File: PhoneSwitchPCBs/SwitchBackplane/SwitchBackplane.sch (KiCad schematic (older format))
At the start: 255 parts, among them J1 Power, J10 UART, J11 SWD, J12 Station 4, J13 Station 8, J2 Station 1, J3 Station 5, J4 Trunk 1, J5 Station 2, J6 Station 6, J7 Trunk 2, J8 Station 3, J9 Station 7, Q1 XP231N02013R-G, Q10 XP231N02013R-G, Q11 XP231N02013R-G, Q12 PMV65XP, Q2 XP231N02013R-G, Q3 XP231N02013R-G, Q4 XP231N02013R-G, Q5 XP231N02013R-G, Q6 XP231N02013R-G, Q7 XP231N02013R-G, Q8 XP231N02013R-G, Q9 XP231N02013R-G, T1 FS28-200-C2, U1 Pi Pico, U10 XRA1403IG24TR-F, U11 TL071, U12 TL071, U13 XRA1403IG24TR-F, U14 XRA1403IG24TR-F, U15 XRA1403IG24TR-F, U2 TL074, U3 TL074, U4 74HC4316, U5 TL071, U6 MT8870DS1, U7 TPA3144D2PWPR, U8 MT8870DS1, U9 74HC4316, Y1 3.579545 MHz

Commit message: Associate footprints with parts, other tweaks
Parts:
- C1, C20, C21, C22, C23, C24, C25, C26, C27, C29, C30, C33, C34, C36, C37, C38, C39, C40, C41, C46, C47, C54, C55, C58, C59: footprint (none) -> Capacitor_SMD:C_1206_3216Metric_Pad1.33x1.80mm_HandSolder
- C10, C15, C43, C44: footprint (none) -> Capacitor_SMD:C_0805_2012Metric_Pad1.18x1.45mm_HandSolder
- C11, C12, C13, C14, C16, C17, C18, C19, C2, C28, C3, C32, C4, C45, C48, C49, C5, C52, C53, C57, C6, C64, C65, C66, C7, C8, C9: footprint (none) -> Capacitor_SMD:C_0603_1608Metric_Pad1.08x0.95mm_HandSolder
- C31, C35: value 1u -> 4.7u; footprint (none) -> Capacitor_SMD:C_1206_3216Metric_Pad1.33x1.80mm_HandSolder
- C42, C56: footprint (none) -> Capacitor_THT:CP_Radial_D6.3mm_P2.50mm
- C50, C51: value 1n -> .001u; footprint (none) -> Capacitor_SMD:C_0603_1608Metric_Pad1.08x0.95mm_HandSolder
- D12, D14, D6: footprint (none) -> LED_SMD:LED_0603_1608Metric_Pad1.05x0.95mm_HandSolder
- D13: value RE1 -> RE6; footprint (none) -> LED_SMD:LED_0603_1608Metric_Pad1.05x0.95mm_HandSolder
- D15: value RT1 -> RT7; footprint (none) -> LED_SMD:LED_0603_1608Metric_Pad1.05x0.95mm_HandSolder
- D16: value RT1 -> RT2; footprint (none) -> LED_SMD:LED_0603_1608Metric_Pad1.05x0.95mm_HandSolder
- D17: value RE1 -> RE7; footprint (none) -> LED_SMD:LED_0603_1608Metric_Pad1.05x0.95mm_HandSolder
- D18: value RE1 -> RE2; footprint (none) -> LED_SMD:LED_0603_1608Metric_Pad1.05x0.95mm_HandSolder
- D19: value RT1 -> RT8; footprint (none) -> LED_SMD:LED_0603_1608Metric_Pad1.05x0.95mm_HandSolder
- D20: value RT1 -> RT3; footprint (none) -> LED_SMD:LED_0603_1608Metric_Pad1.05x0.95mm_HandSolder
- D21: value RE1 -> RE8; footprint (none) -> LED_SMD:LED_0603_1608Metric_Pad1.05x0.95mm_HandSolder
- D24: value RE1 -> RE3; footprint (none) -> LED_SMD:LED_0603_1608Metric_Pad1.05x0.95mm_HandSolder
- D25: value RT1 -> TRT1; footprint (none) -> LED_SMD:LED_0603_1608Metric_Pad1.05x0.95mm_HandSolder
- D26: value RT1 -> RT4; footprint (none) -> LED_SMD:LED_0603_1608Metric_Pad1.05x0.95mm_HandSolder
- D27: value RE1 -> TA1; footprint (none) -> LED_SMD:LED_0603_1608Metric_Pad1.05x0.95mm_HandSolder
- D28: value RE1 -> RE4; footprint (none) -> LED_SMD:LED_0603_1608Metric_Pad1.05x0.95mm_HandSolder
- D29: value RT1 -> TRT2; footprint (none) -> LED_SMD:LED_0603_1608Metric_Pad1.05x0.95mm_HandSolder
- D30: value RT1 -> RT5; footprint (none) -> LED_SMD:LED_0603_1608Metric_Pad1.05x0.95mm_HandSolder
- D31: value RE1 -> TA2; footprint (none) -> LED_SMD:LED_0603_1608Metric_Pad1.05x0.95mm_HandSolder
- D7: value RE1 -> RE5; footprint (none) -> LED_SMD:LED_0603_1608Metric_Pad1.05x0.95mm_HandSolder
- D8: value RT1 -> RGE; footprint (none) -> LED_SMD:LED_0603_1608Metric_Pad1.05x0.95mm_HandSolder
- D9: value RT1 -> RT6; footprint (none) -> LED_SMD:LED_0603_1608Metric_Pad1.05x0.95mm_HandSolder
- J10: renamed from J4; footprint (none) -> Connector_PinSocket_2.54mm:PinSocket_2x11_P2.54mm_Vertical
- J11: renamed from J7; footprint (none) -> Connector_PinSocket_2.54mm:PinSocket_2x11_P2.54mm_Vertical
- J12: renamed from J10; footprint (none) -> Connector_PinHeader_2.54mm:PinHeader_1x03_P2.54mm_Vertical
- J13: renamed from J11; footprint (none) -> Connector_PinHeader_2.54mm:PinHeader_1x03_P2.54mm_Vertical
- J2: footprint (none) -> Connector_PinSocket_2.54mm:PinSocket_2x11_P2.54mm_Vertical
- J3: renamed from J5; footprint (none) -> Connector_PinSocket_2.54mm:PinSocket_2x11_P2.54mm_Vertical
- J4: renamed from J8; footprint (none) -> Connector_PinSocket_2.54mm:PinSocket_2x11_P2.54mm_Vertical
- J5: renamed from J12; footprint (none) -> Connector_PinSocket_2.54mm:PinSocket_2x11_P2.54mm_Vertical
- J6: renamed from J3; footprint (none) -> Connector_PinSocket_2.54mm:PinSocket_2x11_P2.54mm_Vertical
- J7: renamed from J6; footprint (none) -> Connector_PinSocket_2.54mm:PinSocket_2x11_P2.54mm_Vertical
- J8: renamed from J9; footprint (none) -> Connector_PinSocket_2.54mm:PinSocket_2x11_P2.54mm_Vertical
- J9: renamed from J13; footprint (none) -> Connector_PinSocket_2.54mm:PinSocket_2x11_P2.54mm_Vertical
- PS1: footprint OKLT1W12NC -> Imported_Parts:OKLT1W12NC
- PS2: footprint (none) -> Imported_Parts:PDME1S12D5S
- R11, R14, R16, R27, R28, R3, R33, R35, R49, R50, R57, R59, R73, R74, R82, R84, R96, R97: footprint (none) -> Resistor_SMD:R_0805_2012Metric_Pad1.20x1.40mm_HandSolder
- R41, R46, R47, R51, R52, R55, R56, R61, R62, R65, R66, R71, R72, R77, R78, R80, R81, R86, R87, R90, R91: footprint (none) -> Resistor_SMD:R_0603_1608Metric_Pad0.98x0.95mm_HandSolder

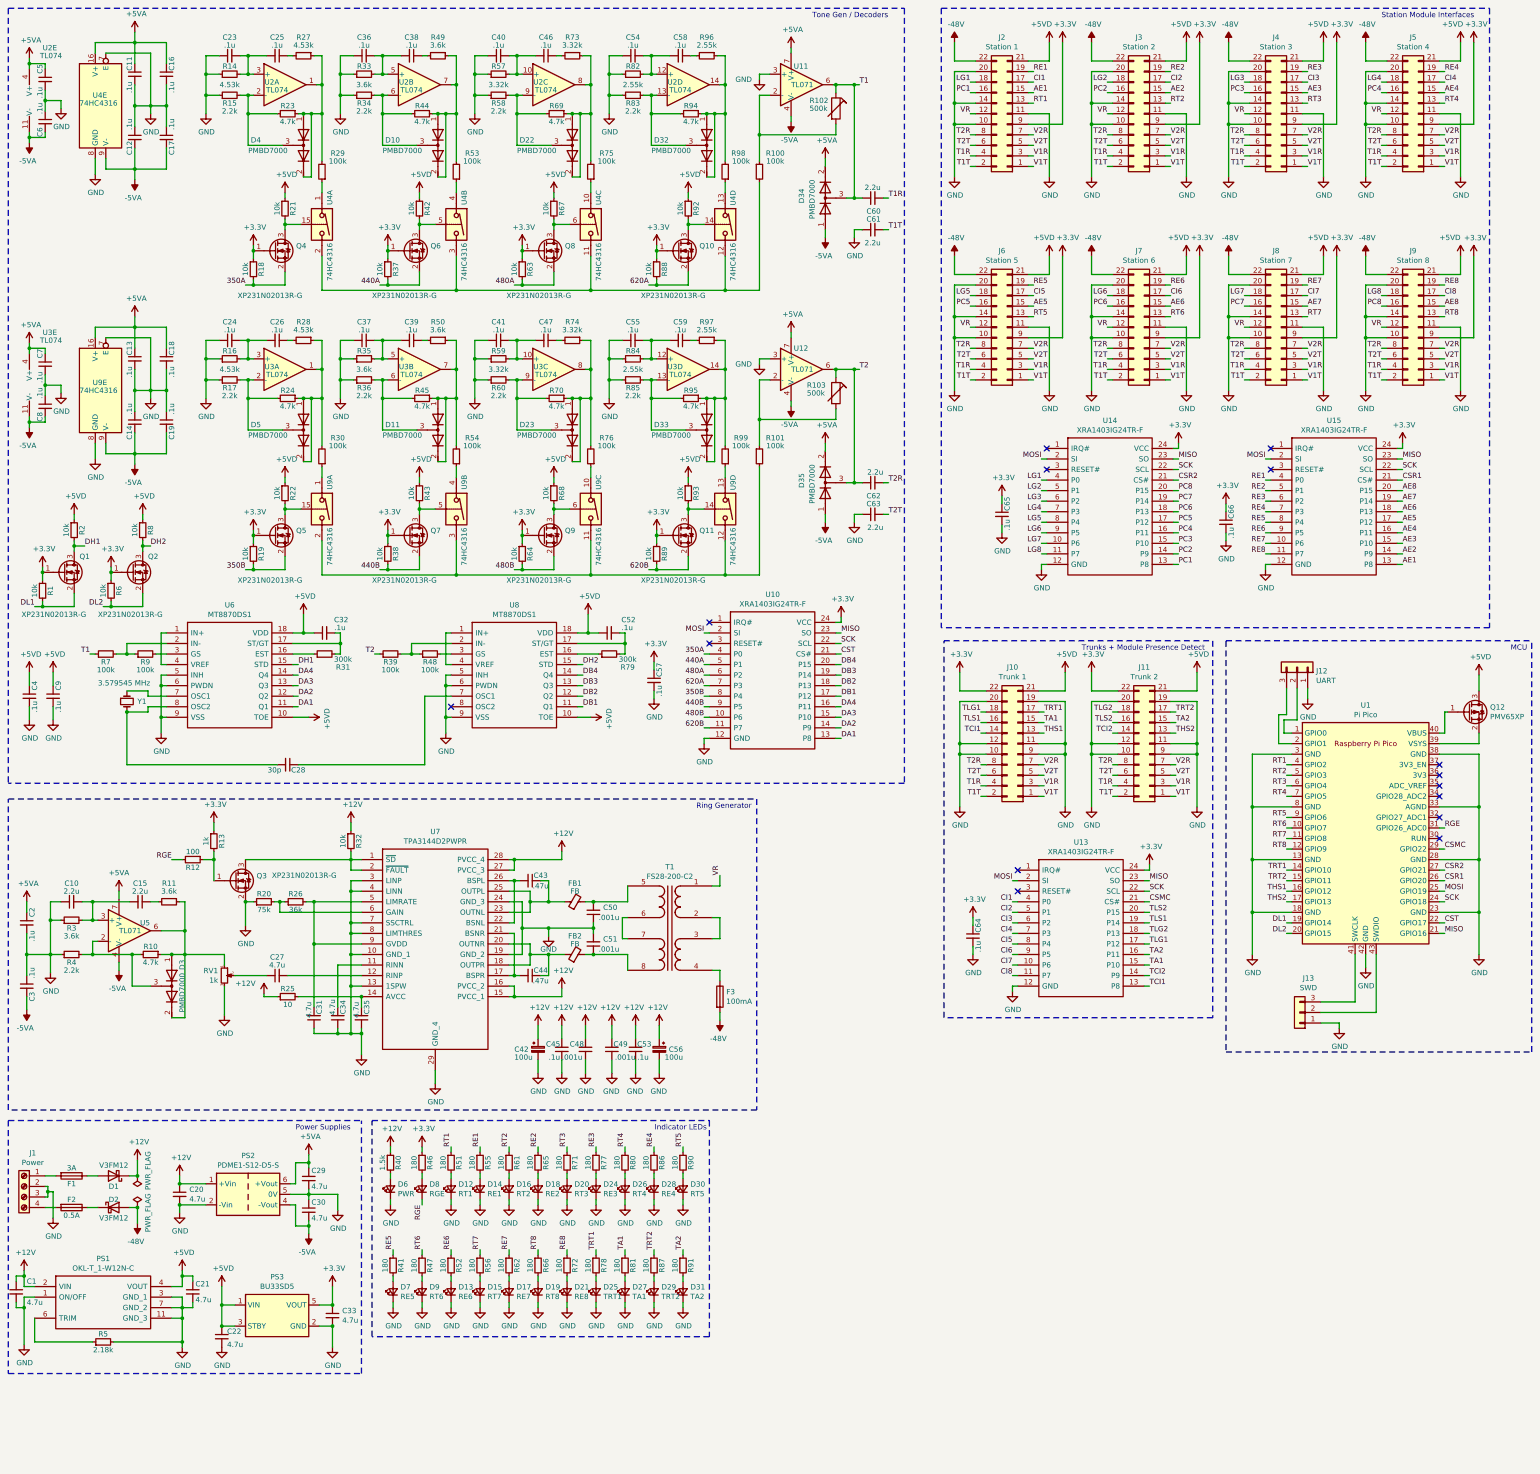
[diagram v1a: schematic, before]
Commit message: Tweaks to schematic, associate all footprints
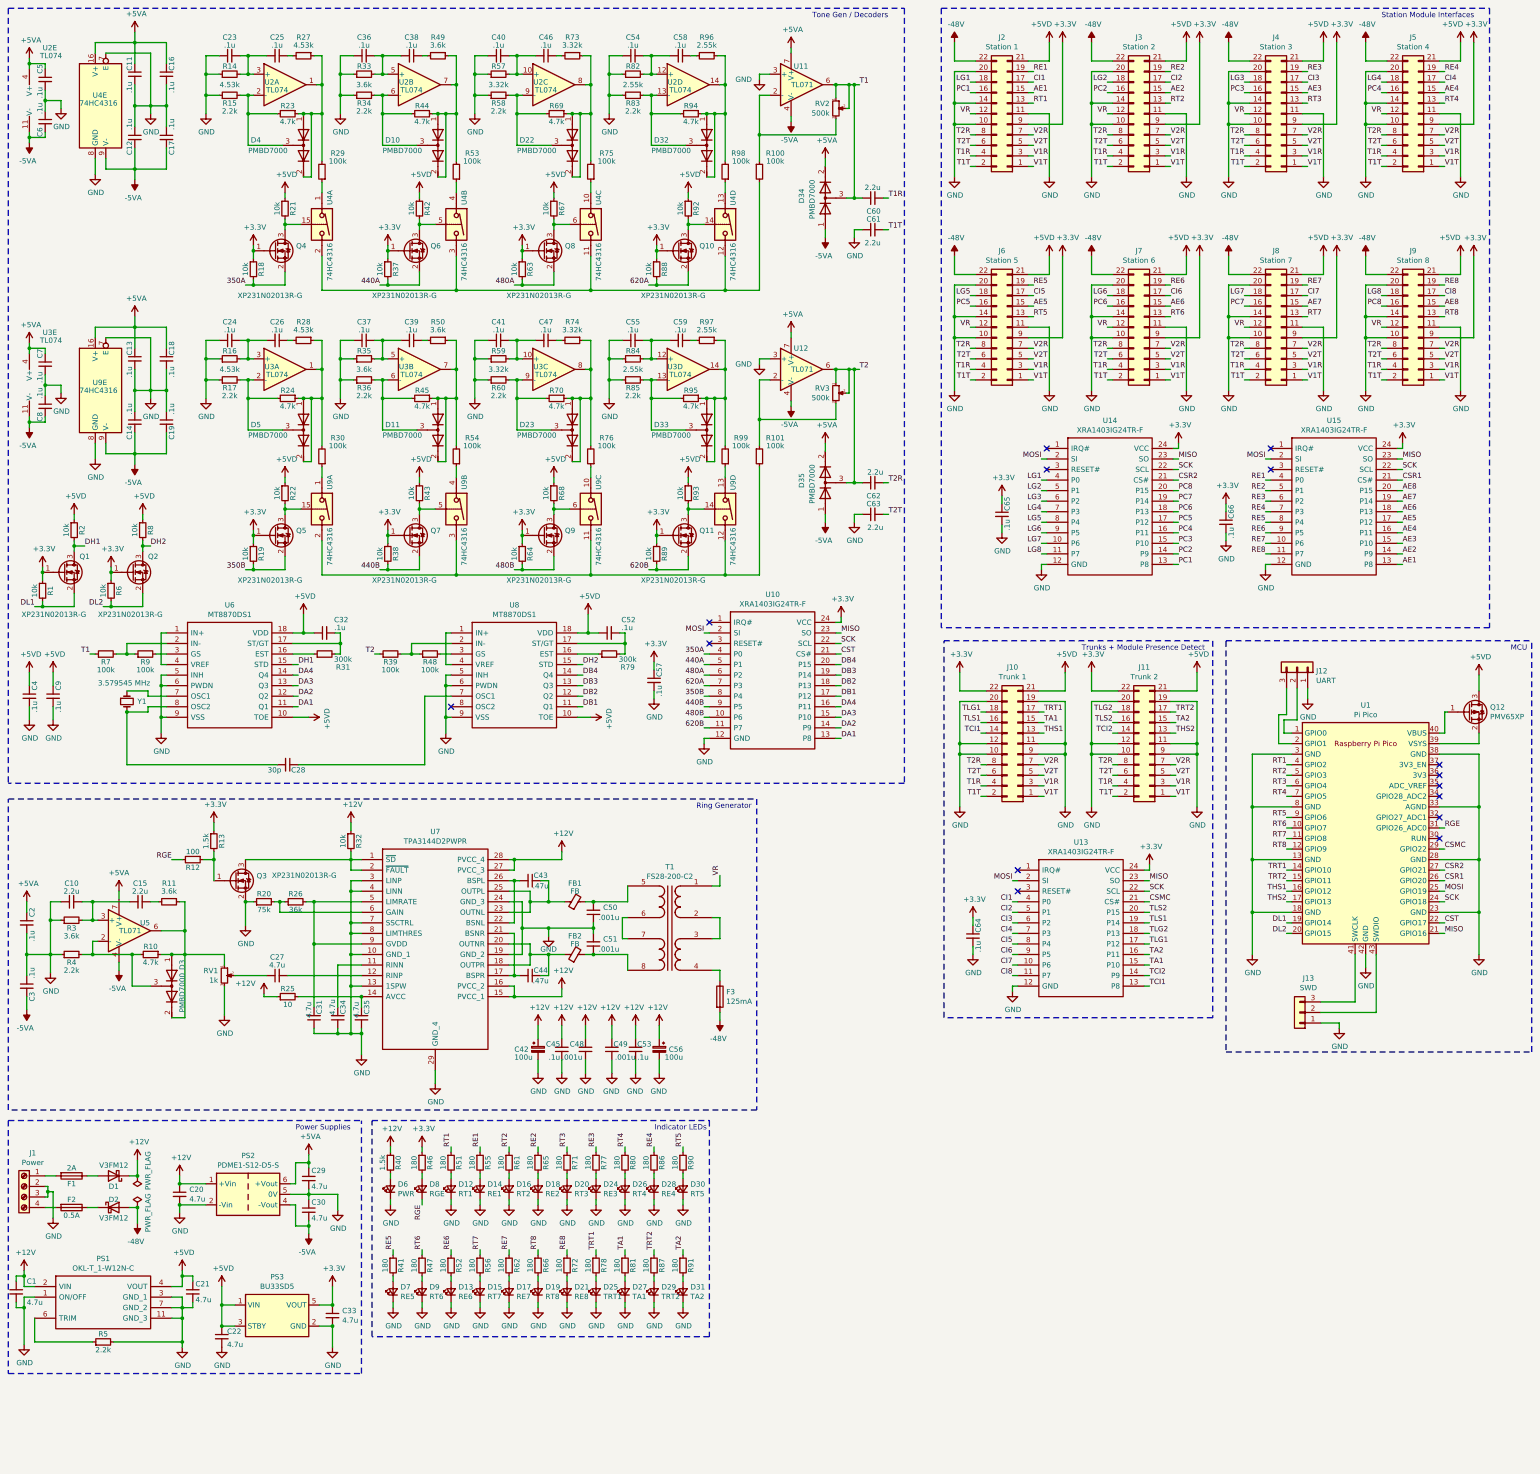
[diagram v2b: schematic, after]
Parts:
- removed R102, R103: 500k, symbol Device:RTRIM
- added RV2, RV3: 500k, Imported_Parts:TC33X-2_1, symbol Device:R_POT_Small
- C60, C61, C62, C63: footprint (none) -> Capacitor_THT:CP_Radial_D6.3mm_P2.50mm
- F1: value 3A -> 2A; footprint (none) -> Imported_Parts:00346605
- F2: footprint (none) -> Imported_Parts:00346605
- F3: value 100mA -> 125mA; footprint (none) -> Imported_Parts:00346605
- FB1, FB2: footprint (none) -> Imported_Parts:NFZ2MSM101SN10B
- J1: footprint (none) -> Imported_Parts:VI0421550000G
- R1, R10, R100, R101, R12, R15, R17, R18, R19, R2, R20, R21, R22, R23, R24, R25, R26, R29, R30, R31, R32, R34, R36, R37, R38, R39, R4, R40, R42, R43, R44, R45, R48, R53, R54, R58, R6, R60, R63, R64, R67, R68, R69, R7, R70, R75, R76, R79, R8, R83, R85, R88, R89, R9, R92, R93, R94, R95, R98, R99: footprint (none) -> Resistor_SMD:R_0805_2012Metric_Pad1.20x1.40mm_HandSolder
- R13: value 1k -> 1.5k; footprint (none) -> Resistor_SMD:R_0805_2012Metric_Pad1.20x1.40mm_HandSolder
- R5: value 2.18k -> 2.2k; footprint (none) -> Resistor_SMD:R_0805_2012Metric_Pad1.20x1.40mm_HandSolder
- RV1: footprint (none) -> Imported_Parts:35WR100KLFTR
- T1: footprint (none) -> Imported_Parts:FS28200C2
- U11, U12, U5: footprint (none) -> Package_SO:SOIC-8_3.9x4.9mm_P1.27mm
- U2, U3: footprint (none) -> Package_SO:SOIC-14_3.9x8.7mm_P1.27mm
- U4, U9: footprint (none) -> Package_SO:SO-16_3.9x9.9mm_P1.27mm
- Y1: footprint (none) -> Crystal:Crystal_SMD_HC49-SD_HandSoldering
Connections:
- net T1: now also RV2.1, RV2.2
- net T2: now also RV3.1, RV3.2
- net at R100.1, U11.2 (-): now also RV2.3
- net at R101.1, U12.2 (-): now also RV3.3

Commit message: Update footprint libraries, fixed broken footprint association
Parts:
- U1: footprint RPi_Pico:RPi_Pico_SMD_TH -> MCU_RaspberryPi_and_Boards:RPi_Pico_SMD_TH
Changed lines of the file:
@@
 F 0 "U1" H 13525 9740 50  0000 C CNN
 F 1 "Pi Pico" H 13525 9649 50  0000 C CNN
-F 2 "RPi_Pico:RPi_Pico_SMD_TH" V 13525 8525 50  0001 C CNN
+F 2 "MCU_RaspberryPi_and_Boards:RPi_Pico_SMD_TH" V 13525 8525 50  0001 C CNN
 F 3 "" H 13525 8525 50  0001 C CNN
 	1    13525 8525

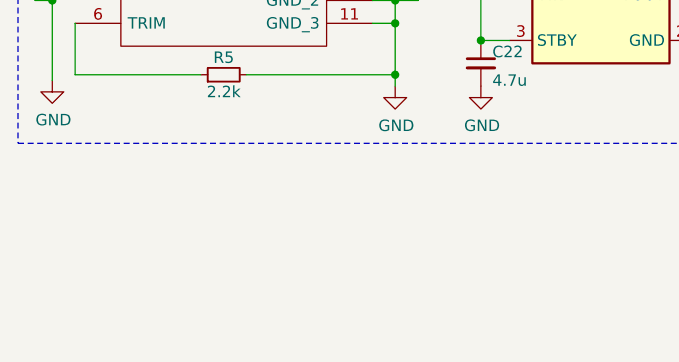
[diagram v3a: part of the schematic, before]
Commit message: Add mounting holes to schematic
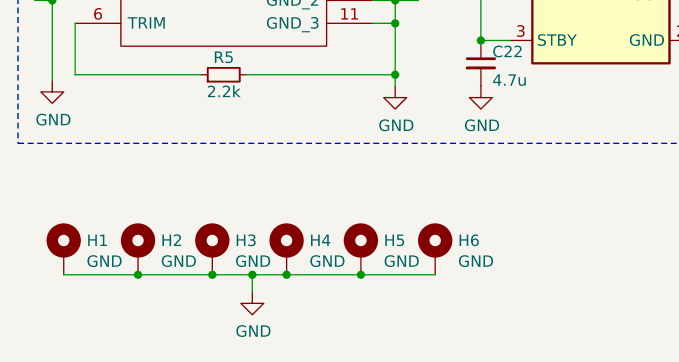
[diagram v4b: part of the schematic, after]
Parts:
- added H1, H2, H3, H4, H5, H6: GND, MountingHole:MountingHole_3.2mm_M3_Pad, symbol Mechanical:MountingHole_Pad
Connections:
- net GND: now also H1.1, H2.1, H3.1, H4.1, H5.1, H6.1
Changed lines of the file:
@@
 Wire Wire Line
 	8500 4450 8500 4600
+$Comp
+L Mechanical:MountingHole_Pad H1
+U 1 1 614C29A5
+P 850 14125
+F 0 "H1" H 950 14174 50  0000 L CNN
+F 1 "GND" H 950 14083 50  0000 L CNN
+F 2 "MountingHole:MountingHole_3.2mm_M3_Pad" H 850 14125 50  0001 C CNN
+F 3 "~" H 850 14125 50  0001 C CNN
+	1    850  14125
+	1    0    0    -1
+$EndComp
+$Comp
+L Mechanical:MountingHole_Pad H2
+U 1 1 614C3473
+P 1175 14125
+F 0 "H2" H 1275 14174 50  0000 L CNN
+F 1 "GND" H 1275 14083 50  0000 L CNN
+F 2 "MountingHole:MountingHole_3.2mm_M3_Pad" H 1175 14125 50  0001 C CNN
+F 3 "~" H 1175 14125 50  0001 C CNN
+	1    1175 14125
+	1    0    0    -1
+$EndComp
+$Comp
+L Mechanical:MountingHole_Pad H3
+U 1 1 614C3737
+P 1500 14125
+F 0 "H3" H 1600 14174 50  0000 L CNN
+F 1 "GND" H 1600 14083 50  0000 L CNN
+F 2 "MountingHole:MountingHole_3.2mm_M3_Pad" H 1500 14125 50  0001 C CNN
+F 3 "~" H 1500 14125 50  0001 C CNN
+	1    1500 14125
+	1    0    0    -1
+$EndComp
+$Comp
+L Mechanical:MountingHole_Pad H4
+U 1 1 614C3AB0
+P 1825 14125
+F 0 "H4" H 1925 14174 50  0000 L CNN
+F 1 "GND" H 1925 14083 50  0000 L CNN
+F 2 "MountingHole:MountingHole_3.2mm_M3_Pad" H 1825 14125 50  0001 C CNN
+F 3 "~" H 1825 14125 50  0001 C CNN
+	1    1825 14125
+	1    0    0    -1
+$EndComp
+$Comp
+L Mechanical:MountingHole_Pad H5
+U 1 1 614C3D3A
+P 2150 14125
+F 0 "H5" H 2250 14174 50  0000 L CNN
+F 1 "GND" H 2250 14083 50  0000 L CNN
+F 2 "MountingHole:MountingHole_3.2mm_M3_Pad" H 2150 14125 50  0001 C CNN
+F 3 "~" H 2150 14125 50  0001 C CNN
+	1    2150 14125
+	1    0    0    -1
+$EndComp
+$Comp
+L Mechanical:MountingHole_Pad H6
+U 1 1 614C405D
+P 2475 14125
+F 0 "H6" H 2575 14174 50  0000 L CNN
+F 1 "GND" H 2575 14083 50  0000 L CNN
+F 2 "MountingHole:MountingHole_3.2mm_M3_Pad" H 2475 14125 50  0001 C CNN
+F 3 "~" H 2475 14125 50  0001 C CNN
+	1    2475 14125
+	1    0    0    -1
+$EndComp
+$Comp
+L power:GND #PWR0202
+U 1 1 614C42F1
+P 1675 14300
+F 0 "#PWR0202" H 1675 14050 50  0001 C CNN
+F 1 "GND" H 1680 14127 50  0000 C CNN
+F 2 "" H 1675 14300 50  0001 C CNN
+F 3 "" H 1675 14300 50  0001 C CNN
+	1    1675 14300
+	1    0    0    -1
+$EndComp
+Wire Wire Line
+	2475 14225 2150 14225
+Connection ~ 1175 14225
+Wire Wire Line
+	1175 14225 850  14225
+Connection ~ 1500 14225
+Wire Wire Line
+	1500 14225 1175 14225
+Connection ~ 1825 14225
+Wire Wire Line
+	1825 14225 1675 14225
+Connection ~ 2150 14225
+Wire Wire Line
+	2150 14225 1825 14225
+Wire Wire Line
+	1675 14300 1675 14225
+Connection ~ 1675 14225
+Wire Wire Line
+	1675 14225 1500 14225
 $EndSCHEMATC

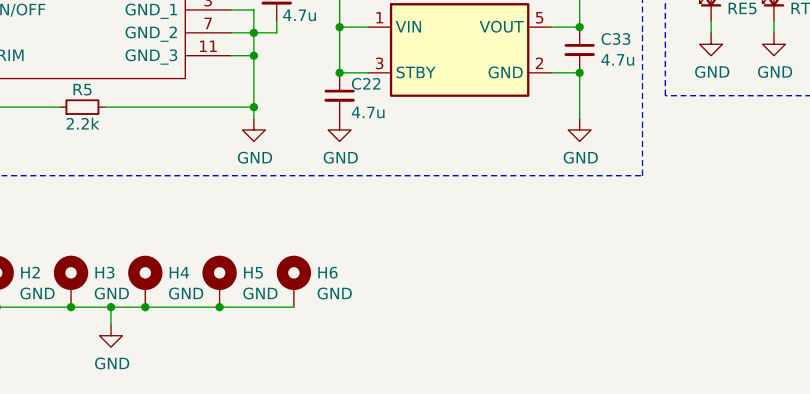
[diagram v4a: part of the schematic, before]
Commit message: Added more mounting holes for transformer
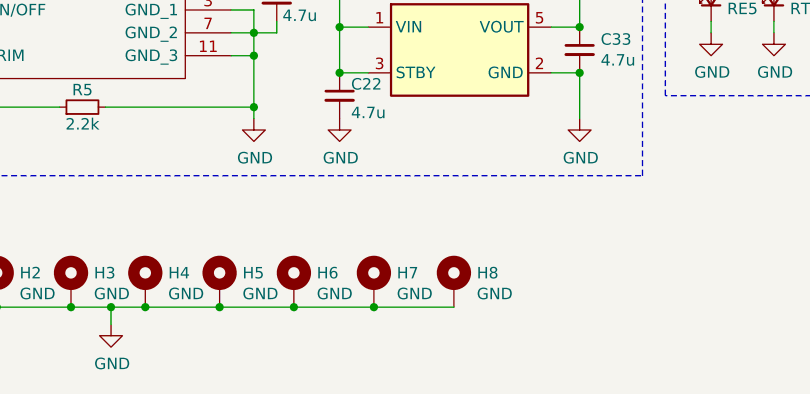
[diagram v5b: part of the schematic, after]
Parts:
- added H7, H8: GND, MountingHole:MountingHole_3.2mm_M3_Pad, symbol Mechanical:MountingHole_Pad
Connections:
- net GND: now also H7.1, H8.1
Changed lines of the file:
@@
 Wire Wire Line
 	1675 14225 1500 14225
+$Comp
+L Mechanical:MountingHole_Pad H7
+U 1 1 618D3DAF
+P 2825 14125
+F 0 "H7" H 2925 14174 50  0000 L CNN
+F 1 "GND" H 2925 14083 50  0000 L CNN
+F 2 "MountingHole:MountingHole_3.2mm_M3_Pad" H 2825 14125 50  0001 C CNN
+F 3 "~" H 2825 14125 50  0001 C CNN
+	1    2825 14125
+	1    0    0    -1
+$EndComp
+$Comp
+L Mechanical:MountingHole_Pad H8
+U 1 1 618D418D
+P 3175 14125
+F 0 "H8" H 3275 14174 50  0000 L CNN
+F 1 "GND" H 3275 14083 50  0000 L CNN
+F 2 "MountingHole:MountingHole_3.2mm_M3_Pad" H 3175 14125 50  0001 C CNN
+F 3 "~" H 3175 14125 50  0001 C CNN
+	1    3175 14125
+	1    0    0    -1
+$EndComp
+Wire Wire Line
+	3175 14225 2825 14225
+Connection ~ 2475 14225
+Connection ~ 2825 14225
+Wire Wire Line
+	2825 14225 2475 14225
 $EndSCHEMATC

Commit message: more PCB chaos
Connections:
- net at C44.1, U7.18 (OUTPR), U7.20 (OUTNR): now also FB1.1; no longer FB2.1
- net at C43.1, U7.23 (OUTNL), U7.25 (OUTPL): now also FB2.1; no longer FB1.1
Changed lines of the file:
@@
 Wire Wire Line
 	5775 8975 5775 9175
-Connection ~ 5775 9175
 Wire Wire Line
 	5500 8975 5450 8975
@@
 Wire Wire Line
 	6125 9175 6200 9175
-Wire Wire Line
-	5775 9175 5925 9175
-Wire Wire Line
-	5925 9675 5775 9675
-Connection ~ 5775 9675
 $Comp
 L Device:C_Small C50
@@
 Wire Wire Line
 	2825 14225 2475 14225
+Wire Wire Line
+	5850 9175 5850 9675
+Wire Wire Line
+	5850 9675 5775 9675
+Connection ~ 5775 9675
+Wire Wire Line
+	5925 9175 5850 9175
+Wire Wire Line
+	5925 9675 5925 9275
+Wire Wire Line
+	5925 9275 5775 9275
+Wire Wire Line
+	5775 9275 5775 9175
+Connection ~ 5775 9175
 $EndSCHEMATC
